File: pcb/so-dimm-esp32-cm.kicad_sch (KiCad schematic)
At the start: 11 parts, among them IC1 PI4IOE5V9535LEX, IC2 PI4IOE5V9535LEX

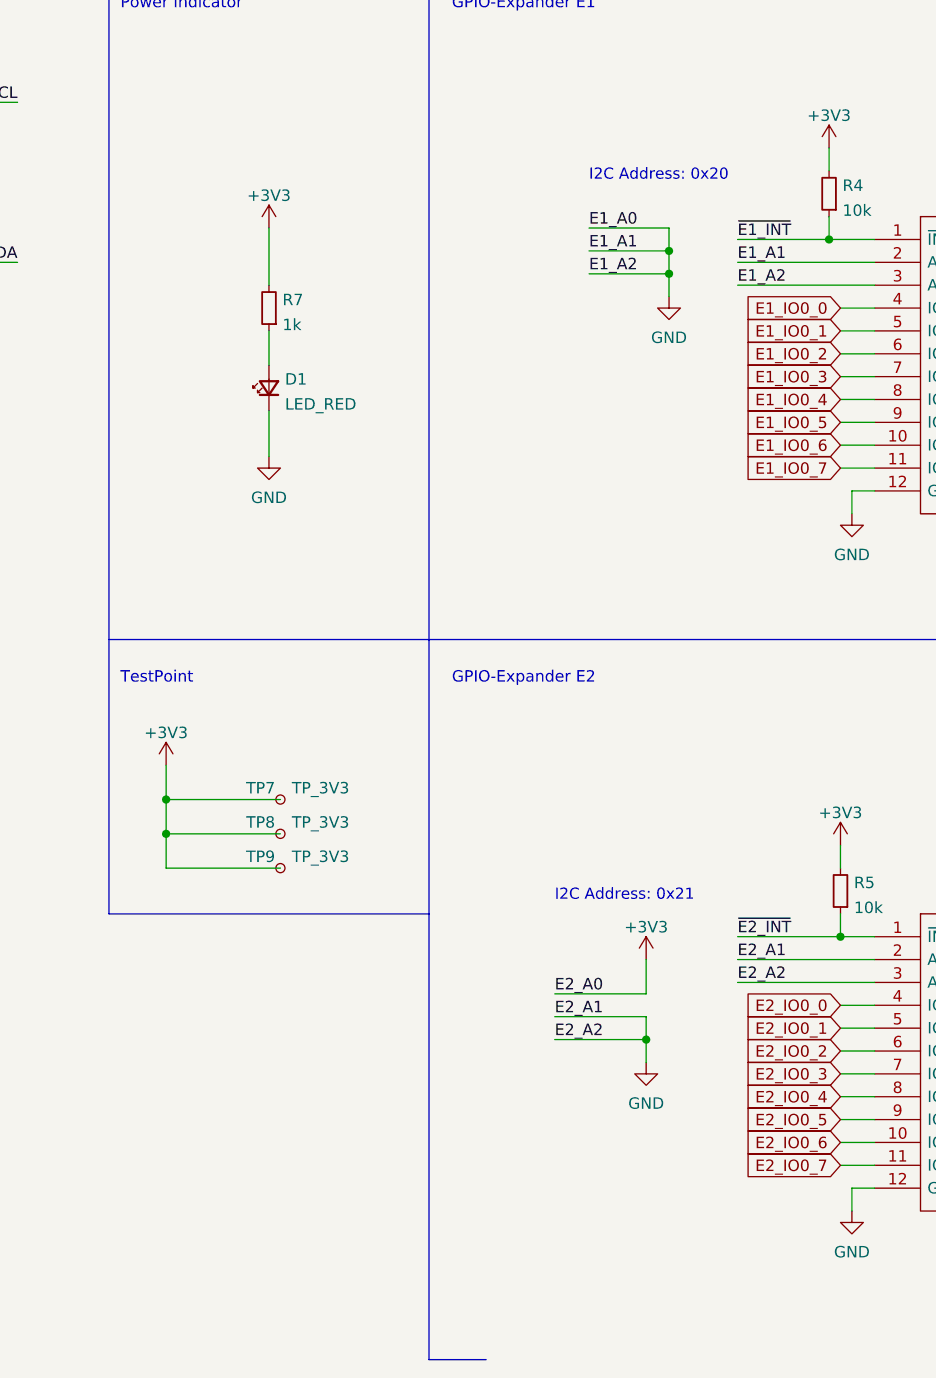
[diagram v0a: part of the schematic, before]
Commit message: Refactored PCB Layer to have one dedicated GND Layer + rerouted traces + removed debug connector and added IO0 to the SO-DIMM connector + added decoupling caps and delay circuit for ESP32 module
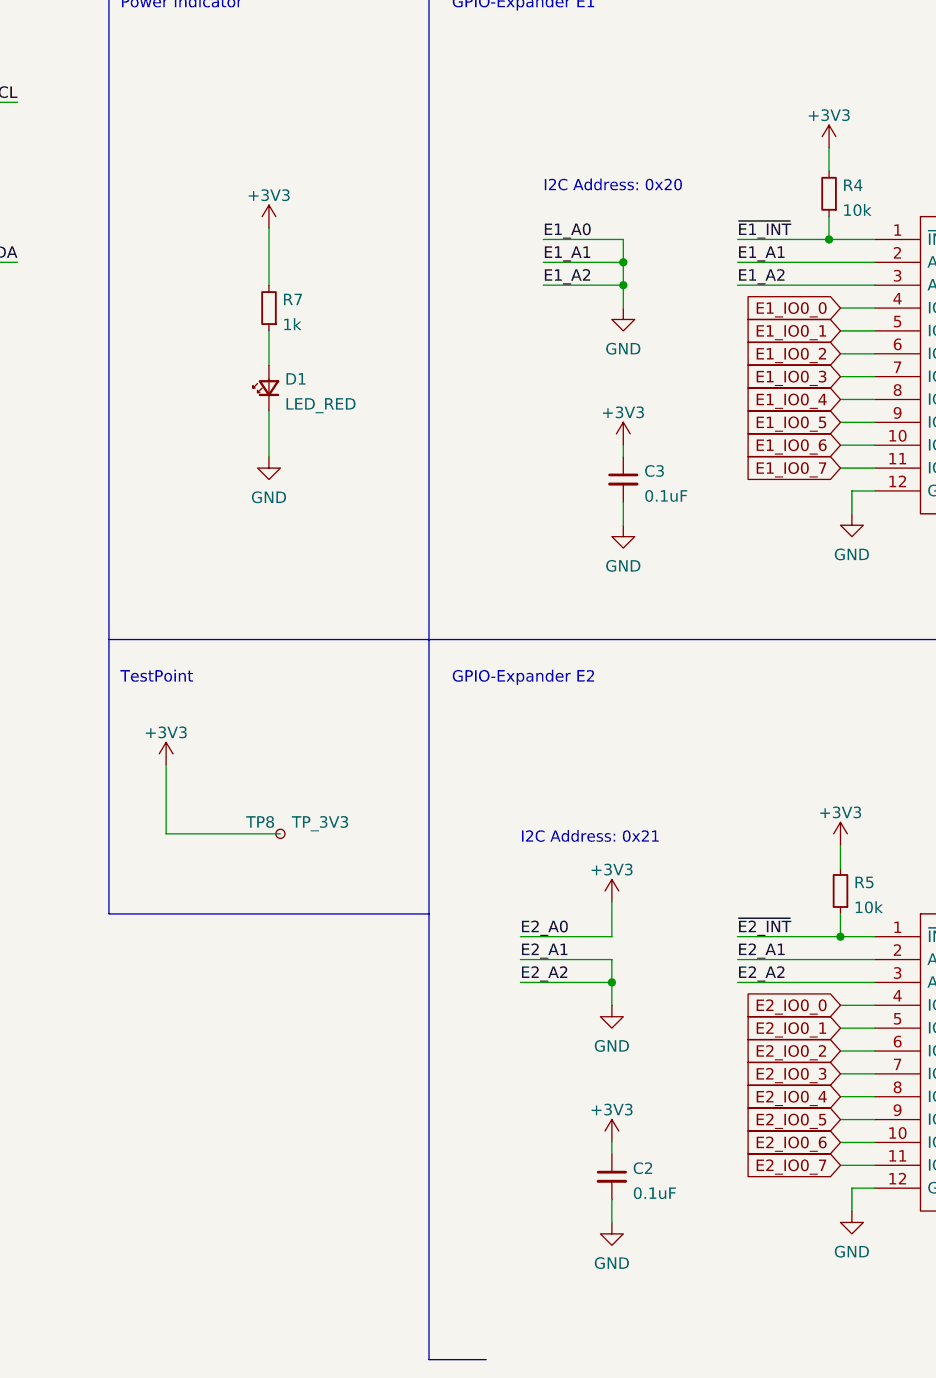
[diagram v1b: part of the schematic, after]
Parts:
- removed TP7, TP9: TP_3V3, TestPoint:TestPoint_Pad_D1.0mm, symbol Connector:TestPoint_Small
- added C2, C3: 0.1uF, Capacitor_SMD:C_0603_1608Metric, symbol Device:C_Small
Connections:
- net +3V3: now also C2.1, C3.1
- net GND: now also C2.2, C3.2

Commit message: Added Datasheet config
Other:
- company: (none) -> OPEN THINGS
- title: (none) -> OPENTHING 1 - ESP-CM3
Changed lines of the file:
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@@
 (kicad_sch (version 20230121) (generator eeschema)
   (paper "A4")
+  (title_block
+    (title "OPENTHING 1 - ESP-CM3")
+    (date "2023-09-11")
+    (rev "REV.03")
+    (company "OPEN THINGS")
+  )
   (junction (at 191.77 46.99) (diameter 0) (color 0 0 0 0)
   )

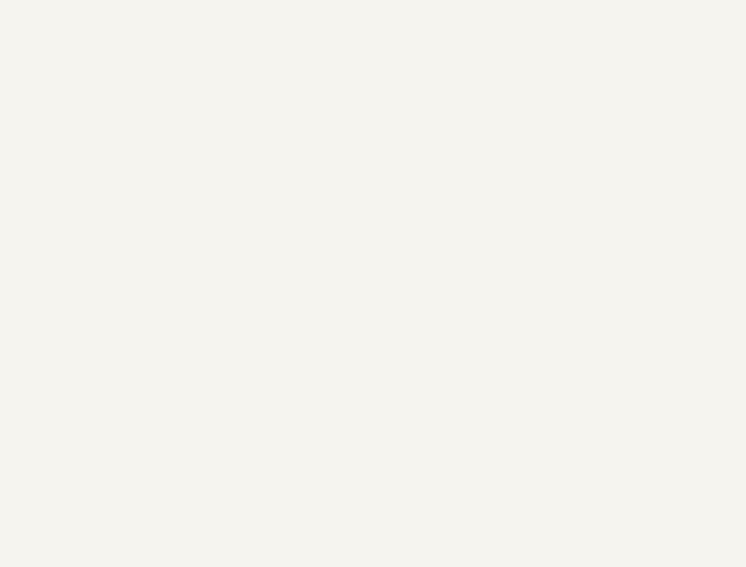
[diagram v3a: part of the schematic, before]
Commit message: Fix SO-DIMM Pinout differences to DDR2 CM3 + Added ground drill
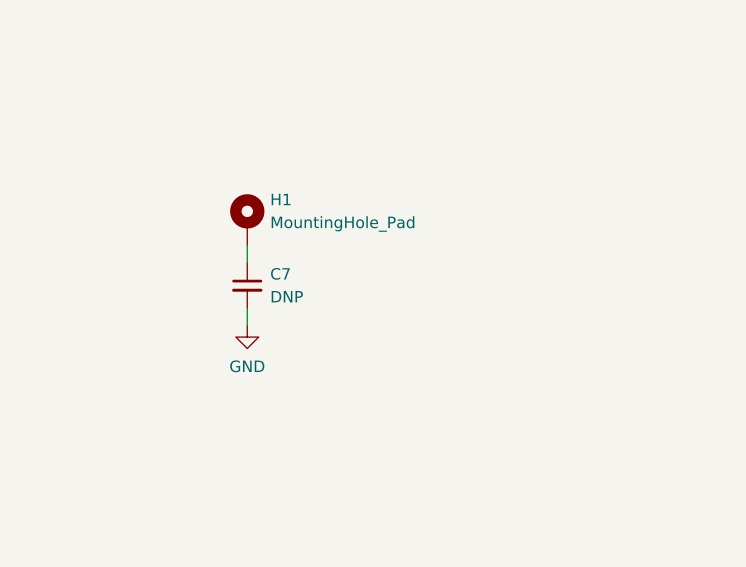
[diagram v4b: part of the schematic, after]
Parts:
- added C7: DNP, Capacitor_SMD:C_0603_1608Metric, symbol Device:C_Small
- added H1: MountingHole_Pad, MountingHole:MountingHole_2.7mm_Pad_Via, symbol Mechanical:MountingHole_Pad
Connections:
- net GND: now also C7.2
- new net: C7.1, H1.1
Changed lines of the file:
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@@
+    (stroke (width 0) (type default))
+  )
+  (wire (pts (xy 58.42 136.525) (xy 58.42 138.43))
     (stroke (width 0) (type default))
   )
@@
   )
   (wire (pts (xy 204.47 46.99) (xy 219.71 46.99))
+    (stroke (width 0) (type default))
+  )
+  (wire (pts (xy 58.42 129.54) (xy 58.42 131.445))
     (stroke (width 0) (type default))
   )
@@
         (path "/e63e39d7-6ac0-4ffd-8aa3-1841a4541b55"
           (reference "#PWR0131") (unit 1)
+        )
+      )
+    )
+  )
+  (symbol (lib_id "power:GND") (at 58.42 138.43 0) (unit 1)
+    (in_bom yes) (on_board yes) (dnp no) (fields_autoplaced)
+    (property "Reference" "#PWR03" (at 58.42 144.78 0)
+      (effects (font (size 1.27 1.27)) hide)
+    )
+    (property "Value" "GND" (at 58.42 142.9925 0)
+      (effects (font (size 1.27 1.27)))
+    )
+    (property "Footprint" "" (at 58.42 138.43 0)
+      (effects (font (size 1.27 1.27)) hide)
+    )
+    (property "Datasheet" "" (at 58.42 138.43 0)
+      (effects (font (size 1.27 1.27)) hide)
+    )
+    (pin "1")
+    (instances
+      (project "so-dimm-esp32-cm"
+        (path "/e63e39d7-6ac0-4ffd-8aa3-1841a4541b55"
+          (reference "#PWR03") (unit 1)
         )
       )
@@
     )
   )
+  (symbol (lib_id "Device:C_Small") (at 58.42 133.985 0) (unit 1)
+    (in_bom yes) (on_board yes) (dnp no) (fields_autoplaced)
+    (property "Reference" "C7" (at 60.96 132.7213 0)
+      (effects (font (size 1.27 1.27)) (justify left))
+    )
+    (property "Value" "DNP" (at 60.96 135.2613 0)
+      (effects (font (size 1.27 1.27)) (justify left))
+    )
+    (property "Footprint" "Capacitor_SMD:C_0603_1608Metric" (at 58.42 133.985 0)
+      (effects (font (size 1.27 1.27)) hide)
+    )
+    (property "Datasheet" "~" (at 58.42 133.985 0)
+      (effects (font (size 1.27 1.27)) hide)
+    )
+    (pin "1")
+    (pin "2")
+    (instances
+      (project "so-dimm-esp32-cm"
+        (path "/e63e39d7-6ac0-4ffd-8aa3-1841a4541b55"
+          (reference "C7") (unit 1)
+        )
+      )
+    )
+  )
   (symbol (lib_id "power:GND") (at 190.5 127 0) (unit 1)
     (in_bom yes) (on_board yes) (dnp no) (fields_autoplaced)
@@
         )
       )
+    )
+  )
+  (symbol (lib_id "Mechanical:MountingHole_Pad") (at 58.42 127 0) (unit 1)
+    (in_bom yes) (on_board yes) (dnp no) (fields_autoplaced)
+    (property "Reference" "H1" (at 60.96 124.46 0)
+      (effects (font (size 1.27 1.27)) (justify left))
+    )
+    (property "Value" "MountingHole_Pad" (at 60.96 127 0)
+      (effects (font (size 1.27 1.27)) (justify left))
+    )
+    (property "Footprint" "MountingHole:MountingHole_2.7mm_Pad_Via" (at 58.42 127 0)
+      (effects (font (size 1.27 1.27)) hide)
+    )
+    (property "Datasheet" "~" (at 58.42 127 0)
+      (effects (font (size 1.27 1.27)) hide)
+    )
+    (pin "1")
+    (instances
+      (project "so-dimm-esp32-cm"
+        (path "/e63e39d7-6ac0-4ffd-8aa3-1841a4541b55"
+          (reference "H1") (unit 1)
+        )
+      )

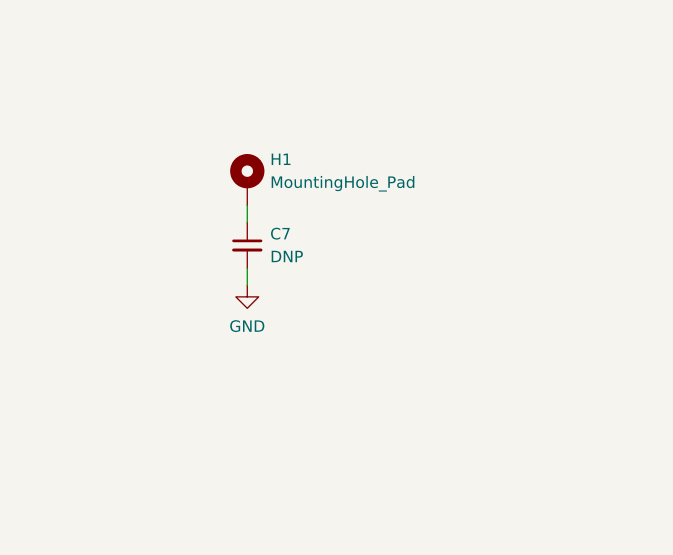
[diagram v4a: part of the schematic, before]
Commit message: Removed parts from BOM and applied clearence changes
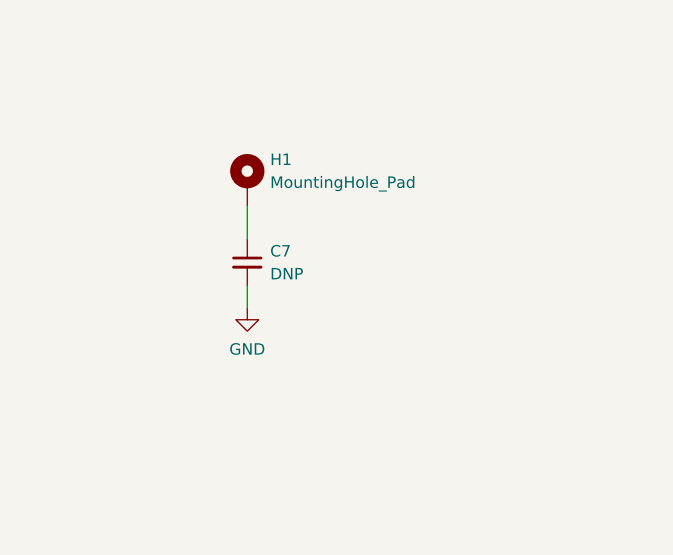
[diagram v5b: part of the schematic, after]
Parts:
- H1, JP1, JP2: now left out of the parts list
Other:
- moved on the sheet: C7
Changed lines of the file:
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@@
+    (stroke (width 0) (type default))
+  )
+  (wire (pts (xy 58.42 138.43) (xy 58.42 140.97))
     (stroke (width 0) (type default))
   )
@@
     (stroke (width 0) (type default))
   )
+  (wire (pts (xy 58.42 129.54) (xy 58.42 133.35))
+    (stroke (width 0) (type default))
+  )
   (wire (pts (xy 256.54 39.37) (xy 256.54 41.91))
     (stroke (width 0) (type default))
@@
     (stroke (width 0) (type default))
   )
-  (wire (pts (xy 58.42 136.525) (xy 58.42 138.43))
-    (stroke (width 0) (type default))
-  )
   (wire (pts (xy 252.73 64.77) (xy 255.27 64.77))
     (stroke (width 0) (type default))
@@
   )
   (wire (pts (xy 204.47 46.99) (xy 219.71 46.99))
-    (stroke (width 0) (type default))
-  )
-  (wire (pts (xy 58.42 129.54) (xy 58.42 131.445))
     (stroke (width 0) (type default))
   )
@@
   )
   (symbol (lib_id "Jumper:SolderJumper_3_Bridged12") (at 110.49 26.67 90) (unit 1)
-    (in_bom yes) (on_board yes) (dnp no) (fields_autoplaced)
+    (in_bom no) (on_board yes) (dnp no) (fields_autoplaced)
     (property "Reference" "JP1" (at 108.8391 25.7615 90)
       (effects (font (size 1.27 1.27)) (justify left))
@@
   )
   (symbol (lib_id "Jumper:SolderJumper_3_Bridged12") (at 110.49 44.45 90) (unit 1)
-    (in_bom yes) (on_board yes) (dnp no) (fields_autoplaced)
+    (in_bom no) (on_board yes) (dnp no) (fields_autoplaced)
     (property "Reference" "JP2" (at 108.8391 43.5415 90)
       (effects (font (size 1.27 1.27)) (justify left))
@@
     )
   )
-  (symbol (lib_id "power:GND") (at 58.42 138.43 0) (unit 1)
-    (in_bom yes) (on_board yes) (dnp no) (fields_autoplaced)
-    (property "Reference" "#PWR03" (at 58.42 144.78 0)
-      (effects (font (size 1.27 1.27)) hide)
-    )
-    (property "Value" "GND" (at 58.42 142.9925 0)
-      (effects (font (size 1.27 1.27)))
-    )
-    (property "Footprint" "" (at 58.42 138.43 0)
-      (effects (font (size 1.27 1.27)) hide)
-    )
-    (property "Datasheet" "" (at 58.42 138.43 0)
+  (symbol (lib_id "power:GND") (at 58.42 140.97 0) (unit 1)
+    (in_bom yes) (on_board yes) (dnp no) (fields_autoplaced)
+    (property "Reference" "#PWR03" (at 58.42 147.32 0)
+      (effects (font (size 1.27 1.27)) hide)
+    )
+    (property "Value" "GND" (at 58.42 145.5325 0)
+      (effects (font (size 1.27 1.27)))
+    )
+    (property "Footprint" "" (at 58.42 140.97 0)
+      (effects (font (size 1.27 1.27)) hide)
+    )
+    (property "Datasheet" "" (at 58.42 140.97 0)
       (effects (font (size 1.27 1.27)) hide)
     )
@@
     )
   )
-  (symbol (lib_id "Device:C_Small") (at 58.42 133.985 0) (unit 1)
-    (in_bom yes) (on_board yes) (dnp no) (fields_autoplaced)
-    (property "Reference" "C7" (at 60.96 132.7213 0)
-      (effects (font (size 1.27 1.27)) (justify left))
-    )
-    (property "Value" "DNP" (at 60.96 135.2613 0)
-      (effects (font (size 1.27 1.27)) (justify left))
-    )
-    (property "Footprint" "Capacitor_SMD:C_0603_1608Metric" (at 58.42 133.985 0)
-      (effects (font (size 1.27 1.27)) hide)
-    )
-    (property "Datasheet" "~" (at 58.42 133.985 0)
+  (symbol (lib_id "Device:C_Small") (at 58.42 135.89 0) (unit 1)
+    (in_bom yes) (on_board yes) (dnp no) (fields_autoplaced)
+    (property "Reference" "C7" (at 60.96 134.6263 0)
+      (effects (font (size 1.27 1.27)) (justify left))
+    )
+    (property "Value" "DNP" (at 60.96 137.1663 0)
+      (effects (font (size 1.27 1.27)) (justify left))
+    )
+    (property "Footprint" "Capacitor_SMD:C_0603_1608Metric" (at 58.42 135.89 0)
+      (effects (font (size 1.27 1.27)) hide)
+    )
+    (property "Datasheet" "~" (at 58.42 135.89 0)
       (effects (font (size 1.27 1.27)) hide)
     )
@@
   )
   (symbol (lib_id "Mechanical:MountingHole_Pad") (at 58.42 127 0) (unit 1)
-    (in_bom yes) (on_board yes) (dnp no) (fields_autoplaced)
+    (in_bom no) (on_board yes) (dnp no) (fields_autoplaced)
     (property "Reference" "H1" (at 60.96 124.46 0)
       (effects (font (size 1.27 1.27)) (justify left))
